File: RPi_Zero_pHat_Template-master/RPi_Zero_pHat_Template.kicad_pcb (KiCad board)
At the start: 2 copper layers, 65 x 30.5 mm, 6 parts, among them J1 RPi_GPIO, J2 RPi_GPIO

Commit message: -remove smd header; -add resistor
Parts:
- removed J1: RPi_GPIO, Connector_Samtec_HLE_SMD-ML:Samtec_HLE-120-02-xxx-DV-BE-A_2x20_RPi_Bottom
- added R1: R, Resistors_SMD:R_0603_1608Metric, F.Cu at (48.3, 38.6)
- J2: footprint Connector_PinHeader_2.54mm:PinHeader_2x20_P2.54mm_Vertical -> Pin_Headers:PinHeader_2x20_P2.54mm_Vertical

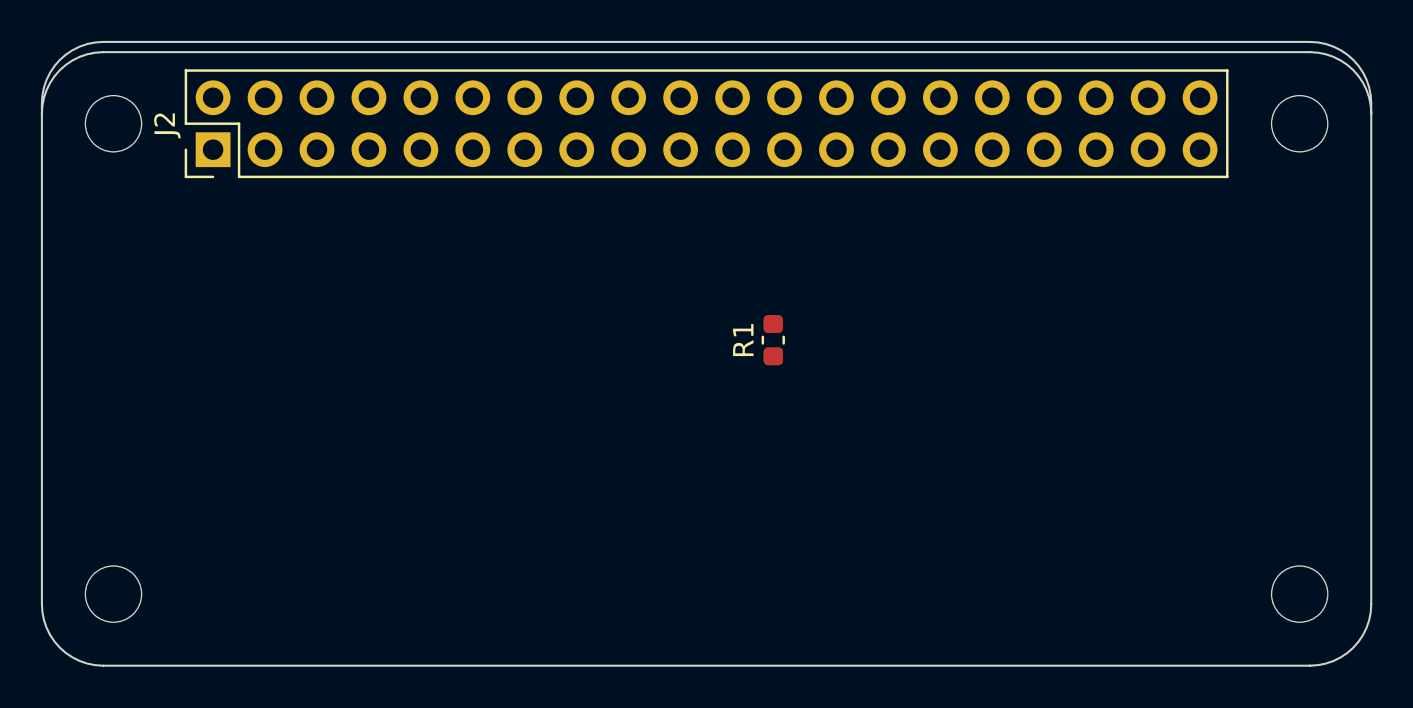
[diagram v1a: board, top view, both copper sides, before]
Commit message: -edit 3D PCB view
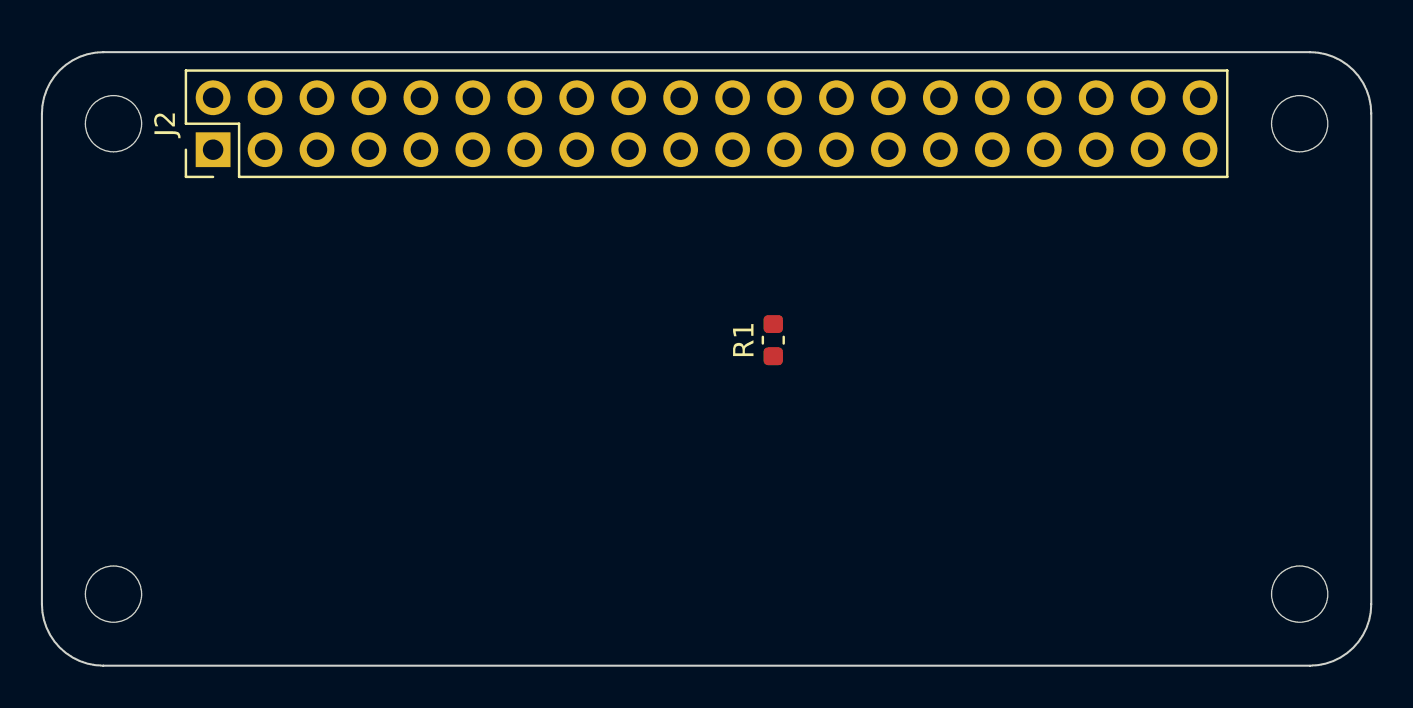
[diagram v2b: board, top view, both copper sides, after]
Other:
- board size 65 x 30.5 mm -> 65 x 30 mm
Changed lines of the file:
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@@
   (general
     (thickness 1.6)
-    (drawings 20)
+    (drawings 17)
     (tracks 0)
     (zones 0)
@@
   (gr_arc (start 74.5 51.5) (end 77.5 51.5) (angle 90) (layer Edge.Cuts) (width 0.1))
   (gr_arc (start 15.5 51.5) (end 15.5 54.5) (angle 90) (layer Edge.Cuts) (width 0.1))
-  (gr_arc (start 15.5 27) (end 12.5 27) (angle 90) (layer Edge.Cuts) (width 0.1))
-  (gr_arc (start 74.5 27) (end 74.5 24) (angle 90) (layer Edge.Cuts) (width 0.1))
-  (gr_line (start 12.5 27) (end 12.5 51.5) (layer Edge.Cuts) (width 0.1))
+  (gr_line (start 12.5 27.5) (end 12.5 51.5) (layer Edge.Cuts) (width 0.1))
   (gr_line (start 15.5 54.5) (end 74.5 54.5) (angle 90) (layer Edge.Cuts) (width 0.1))
-  (gr_line (start 77.5 27) (end 77.5 51.5) (angle 90) (layer Edge.Cuts) (width 0.1))
-  (gr_line (start 15.5 24) (end 74.5 24) (angle 90) (layer Edge.Cuts) (width 0.1))
+  (gr_line (start 77.5 27.5) (end 77.5 51.5) (angle 90) (layer Edge.Cuts) (width 0.1))
 )
